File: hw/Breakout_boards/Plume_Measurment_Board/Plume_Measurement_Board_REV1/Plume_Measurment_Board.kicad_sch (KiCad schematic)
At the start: 19 parts, among them U2 LMP7721MA/NOPB, U3 LMP2022MA/NOPB, U4 AD8475ARMZ, U5 AD8475ARMZ, U7 AD7176-2BRUZ

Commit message: Schematic Progress Buffer/2nd Stage Amplifier Integration
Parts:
- added C14: 10uF, Capacitor_SMD:C_0805_2012Metric_Pad1.18x1.45mm_HandSolder, symbol Device:C
- added C15: 100nF, Capacitor_SMD:C_0603_1608Metric_Pad1.08x0.95mm_HandSolder, symbol Device:C
- added C16: 1uF, Capacitor_SMD:C_0805_2012Metric_Pad1.18x1.45mm_HandSolder, symbol Device:C
- added R10, R9: ?, Resistor_SMD:R_0603_1608Metric_Pad0.98x0.95mm_HandSolder, symbol Device:R_US
- added R11, R12: 1000, Resistor_SMD:R_0603_1608Metric_Pad0.98x0.95mm_HandSolder, symbol Device:R_US
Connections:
- net VSS is gone; now on net GND: C11.2, C12.1, C13.1, C4.2, U7.6 (AVSS)
- net +2.5V: now also U3.3 (INA+), U4.1 (IN0.8X-), U5.1 (IN0.8X-)
- net +3V3: now also U7.16 (IOVDD), C14.2, C15.2
- net +5V: now also U3.8 (V+), U4.3 (VS+), U5.3 (VS+)
- net GND: now also U3.4 (V-), U4.8 (VS-), U5.8 (VS-), U7.17 (DGND), C14.1, C15.1, C16.1
- net at U7.18 (REGCAPD): now also C16.2
- net 1_IN0.8+: now reaches U4.10 (IN0.8X+)
- net 1_IN0.8+: now also U3.1 (OUTA), R11.2
- net at U3.2 (INA-): now also R11.1, R12.2
- net 2_IN0.8+: now reaches U5.10 (IN0.8X+)
- new net Amplified_Plume_1: R12.1
- no-connect marks 3 -> 12
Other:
- note added: "GND Power Connection"
- moved on the sheet: R7, R8

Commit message: Schematic Finished
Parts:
- added C17: .1pF, Capacitor_SMD:C_0402_1005Metric_Pad0.74x0.62mm_HandSolder, symbol Device:C
- added R13: 1G, Resistor_SMD:R_2512_6332Metric_Pad1.40x3.35mm_HandSolder, symbol Device:R_US
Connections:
- net +2.5V: now also U2.2 (NC), U2.7 (NC), U3.5 (INB+)
- net +5V: now also U2.6 (V+)
- net 2_IN0.8+: now also R9.2, U3.7 (OUTB)
- net Amplified_Plume_1: now also R10.1, U2.4 (OUT), C17.2, R13.1
- net GND: now also U2.1 (IN+), U2.3 (V-)
- net Plume: now also U2.8 (IN-), C17.1, R13.2
- net at U3.6 (INB-): now also R10.2, R9.1
- no-connect marks 12 -> 13
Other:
- moved on the sheet: R10, R9, U2

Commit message: Good Routing Progress
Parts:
- added C18: 1uF, Capacitor_SMD:C_0805_2012Metric_Pad1.18x1.45mm_HandSolder, symbol Device:C
- added C19: 1uF, Capacitor_SMD:C_0603_1608Metric_Pad1.08x0.95mm_HandSolder, symbol Device:C
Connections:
- net +2.5V: now also C10.1, C5.2, C6.1, C9.2, C18.2, C19.1
- net +5V: now also C19.2
- net GND: now also C18.1; no longer C10.1, C5.2, C6.1, C9.2
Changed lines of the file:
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@@
 	)
 	(junction
+		(at 110.49 180.34)
+		(diameter 0)
+		(color 0 0 0 0)
+	)
+	(junction
 		(at 175.26 125.73)
 		(diameter 0)
@@
 	(wire
 		(pts
+			(xy 110.49 168.91) (xy 110.49 171.45)
+		)
+		(stroke
+			(width 0)
+			(type default)
+		)
+	)
+	(wire
+		(pts
 			(xy 74.93 34.29) (xy 74.93 53.34)
 		)
@@
 	(wire
 		(pts
+			(xy 110.49 189.23) (xy 110.49 194.31)
+		)
+		(stroke
+			(width 0)
+			(type default)
+		)
+	)
+	(wire
+		(pts
 			(xy 262.89 113.03) (xy 262.89 114.3)
 		)
@@
 	(wire
 		(pts
+			(xy 110.49 180.34) (xy 110.49 181.61)
+		)
+		(stroke
+			(width 0)
+			(type default)
+		)
+	)
+	(wire
+		(pts
 			(xy 62.23 26.67) (xy 74.93 26.67)
 		)
@@
 	(wire
 		(pts
+			(xy 102.87 180.34) (xy 110.49 180.34)
+		)
+		(stroke
+			(width 0)
+			(type default)
+		)
+	)
+	(wire
+		(pts
 			(xy 91.44 111.76) (xy 96.52 111.76)
 		)
@@
 	(wire
 		(pts
+			(xy 110.49 179.07) (xy 110.49 180.34)
+		)
+		(stroke
+			(width 0)
+			(type default)
+		)
+	)
+	(wire
+		(pts
 			(xy 147.32 97.79) (xy 147.32 100.33)
 		)
@@
 		)
 	)
+	(hierarchical_label "+2.5V"
+		(shape input)
+		(at 269.24 93.98 0)
+		(effects
+			(font
+				(size 1.27 1.27)
+			)
+			(justify left)
+		)
+	)
 	(hierarchical_label "VSS"
 		(shape input)
@@
 		)
 	)
+	(hierarchical_label "+2.5V"
+		(shape input)
+		(at 274.32 114.3 0)
+		(effects
+			(font
+				(size 1.27 1.27)
+			)
+			(justify left)
+		)
+	)
+	(hierarchical_label "+2.5V"
+		(shape input)
+		(at 102.87 180.34 180)
+		(effects
+			(font
+				(size 1.27 1.27)
+			)
+			(justify right)
+		)
+	)
 	(hierarchical_label "+OUT_2"
 		(shape input)
@@
 		)
 	)
+	(hierarchical_label "VSS"
+		(shape input)
+		(at 110.49 194.31 180)
+		(effects
+			(font
+				(size 1.27 1.27)
+			)
+			(justify right)
+		)
+	)
 	(hierarchical_label "+2.5V"
 		(shape input)
@@
 	)
 	(symbol
-		(lib_id "power:GND")
-		(at 274.32 114.3 0)
+		(lib_id "power:+3V3")
+		(at 110.49 168.91 0)
 		(unit 1)
 		(body_style 1)
@@
 		(in_pos_files yes)
 		(dnp no)
-		(fields_autoplaced yes)
-		(property "Reference" "#PWR07"
-			(at 274.32 120.65 0)
+		(property "Reference" "#PWR0255"
+			(at 110.49 172.72 0)
 			(hide yes)
 			(show_name no)
@@
 			)
 		)
-		(property "Value" "GND"
-			(at 274.32 119.38 0)
+		(property "Value" "+5V"
+			(at 110.236 165.1 0)
 			(show_name no)
 			(do_not_autoplace no)
@@
 		)
 		(property "Footprint" ""
-			(at 274.32 114.3 0)
+			(at 110.49 168.91 0)
 			(hide yes)
 			(show_name no)
@@
 		)
 		(property "Datasheet" ""
-			(at 274.32 114.3 0)
+			(at 110.49 168.91 0)
 			(hide yes)
 			(show_name no)
@@
 			)
 		)
-		(property "Description" "Power symbol creates a global label with name \"GND\" , ground"
-			(at 274.32 114.3 0)
+		(property "Description" "Power symbol creates a global label with name \"+3V3\""
+			(at 110.49 168.91 0)
 			(hide yes)
 			(show_name no)
@@
 			(project "Plume_Measurment_Board"
 				(path "/2e1d3673-27b9-4604-80fb-036cec98a912"
-					(reference "#PWR07")
+					(reference "#PWR0255")
 					(unit 1)
 				)
@@
 	)
 	(symbol
+		(lib_id "Device:C")
+		(at 110.49 175.26 180)
+		(unit 1)
+		(body_style 1)
+		(exclude_from_sim no)
+		(in_bom yes)
+		(on_board yes)
+		(in_pos_files yes)
+		(dnp no)
+		(property "Reference" "C19"
+			(at 113.284 173.482 0)
+			(show_name no)
+			(do_not_autoplace no)
+			(effects
+				(font
+					(size 1.27 1.27)
+				)
+				(justify right)
+			)
+		)
+		(property "Value" "1uF"
+			(at 113.284 176.022 0)
+			(show_name no)
+			(do_not_autoplace no)
+			(effects
+				(font
+					(size 1.27 1.27)
+				)
+				(justify right)
+			)
+		)
+		(property "Footprint" "Capacitor_SMD:C_0603_1608Metric_Pad1.08x0.95mm_HandSolder"
+			(at 109.5248 171.45 0)
+			(hide yes)
+			(show_name no)
+			(do_not_autoplace no)
+			(effects
+				(font
+					(size 1.27 1.27)
+				)
+			)
+		)
+		(property "Datasheet" ""
+			(at 110.49 175.26 0)
+			(hide yes)
+			(show_name no)
+			(do_not_autoplace no)
+			(effects
+				(font
+					(size 1.27 1.27)
+				)
+			)
+		)
+		(property "Description" "Unpolarized capacitor"
+			(at 110.49 175.26 0)
+			(hide yes)
+			(show_name no)
+			(do_not_autoplace no)
+			(effects
+				(font
+					(size 1.27 1.27)
+				)
+			)
+		)
+		(pin "2"
+		)
+		(pin "1"
+		)
+		(instances
+			(project "Plume_Measurment_Board"
+				(path "/2e1d3673-27b9-4604-80fb-036cec98a912"
+					(reference "C19")
+					(unit 1)
+				)
+			)
+		)
+	)
+	(symbol
 		(lib_id "ADC_Analog_Devices:AD7176-2BRUZ")
 		(at 177.8 110.49 0)
@@
 	)
 	(symbol
+		(lib_id "Device:C")
+		(at 110.49 185.42 180)
+		(unit 1)
+		(body_style 1)
+		(exclude_from_sim no)
+		(in_bom yes)
+		(on_board yes)
+		(in_pos_files yes)
+		(dnp no)
+		(property "Reference" "C18"
+			(at 103.632 183.896 0)
+			(show_name no)
+			(do_not_autoplace no)
+			(effects
+				(font
+					(size 1.27 1.27)
+				)
+				(justify right)
+			)
+		)
+		(property "Value" "1uF"
+			(at 103.632 186.436 0)
+			(show_name no)
+			(do_not_autoplace no)
+			(effects
+				(font
+					(size 1.27 1.27)
+				)
+				(justify right)
+			)
+		)
+		(property "Footprint" "Capacitor_SMD:C_0805_2012Metric_Pad1.18x1.45mm_HandSolder"
+			(at 109.5248 181.61 0)
+			(hide yes)
+			(show_name no)
+			(do_not_autoplace no)
+			(effects
+				(font
+					(size 1.27 1.27)
+				)
+			)
+		)
+		(property "Datasheet" ""
+			(at 110.49 185.42 0)
+			(hide yes)
+			(show_name no)
+			(do_not_autoplace no)
+			(effects
+				(font
+					(size 1.27 1.27)
+				)
+			)
+		)
+		(property "Description" "Unpolarized capacitor"
+			(at 110.49 185.42 0)
+			(hide yes)
+			(show_name no)
+			(do_not_autoplace no)
+			(effects
+				(font
+					(size 1.27 1.27)
+				)
+			)
+		)
+		(pin "2"
+		)
+		(pin "1"
+		)
+		(instances
+			(project "Plume_Measurment_Board"
+				(path "/2e1d3673-27b9-4604-80fb-036cec98a912"
+					(reference "C18")
+					(unit 1)
+				)
+			)
+		)
+	)
+	(symbol
 		(lib_id "Device:R_US")
 		(at 269.24 102.87 90)
@@
 					(unit 1)
 				)
-			)
-		)
-	)
-	(symbol
-		(lib_id "power:GND")
-		(at 269.24 93.98 0)
-		(unit 1)
-		(body_style 1)
-		(exclude_from_sim no)
-		(in_bom yes)
-		(on_board yes)
-		(in_pos_files yes)
-		(dnp no)
-		(property "Reference" "#PWR06"
-			(at 269.24 100.33 0)
-			(hide yes)
-			(show_name no)
-			(do_not_autoplace no)
-			(effects
-				(font
-					(size 1.27 1.27)
-				)
-			)
-		)
-		(property "Value" "GND"
-			(at 265.43 96.012 0)
-			(show_name no)
-			(do_not_autoplace no)
-			(effects
-				(font
-					(size 1.27 1.27)
-				)
-			)
-		)
-		(property "Footprint" ""
-			(at 269.24 93.98 0)
-			(hide yes)
-			(show_name no)
-			(do_not_autoplace no)
-			(effects
-				(font
-					(size 1.27 1.27)
-				)
-			)
-		)
-		(property "Datasheet" ""
-			(at 269.24 93.98 0)
-			(hide yes)
-			(show_name no)
-			(do_not_autoplace no)
-			(effects
-				(font
-					(size 1.27 1.27)
-				)
-			)
-		)
-		(property "Description" "Power symbol creates a global label with name \"GND\" , ground"
-			(at 269.24 93.98 0)
-			(hide yes)
-			(show_name no)
-			(do_not_autoplace no)
-			(effects
-				(font
-					(size 1.27 1.27)
-				)
-			)
-		)
-		(pin "1"
-		)
-		(instances
-			(project "Plume_Measurment_Board"
-				(path "/2e1d3673-27b9-4604-80fb-036cec98a912"
-					(reference "#PWR06")
-					(unit 1)
-				)

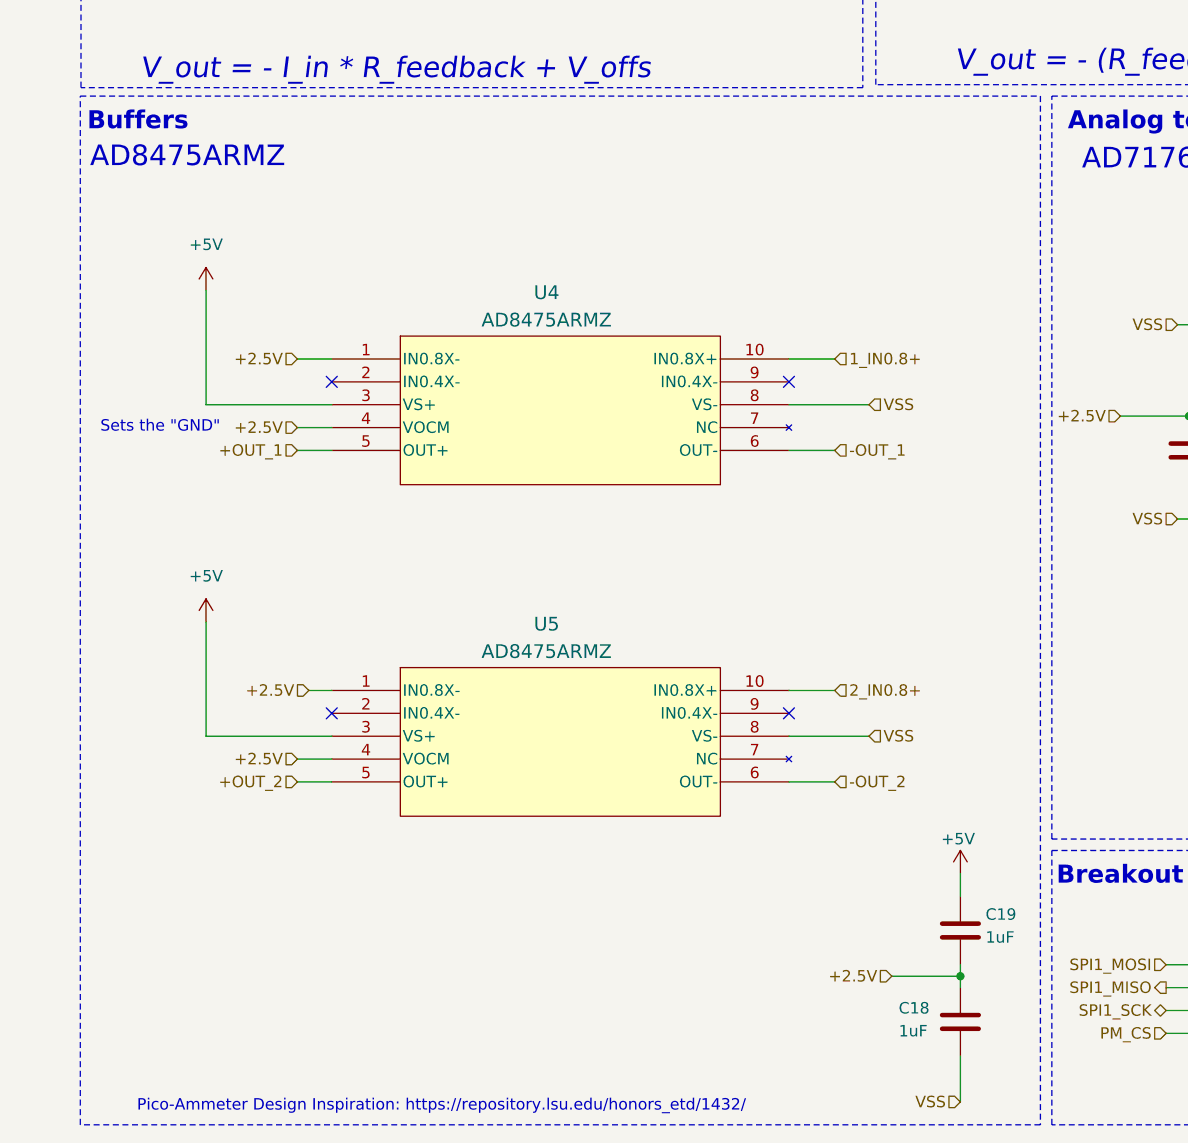
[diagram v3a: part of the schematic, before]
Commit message: MAX31856 Driver Full Integrations
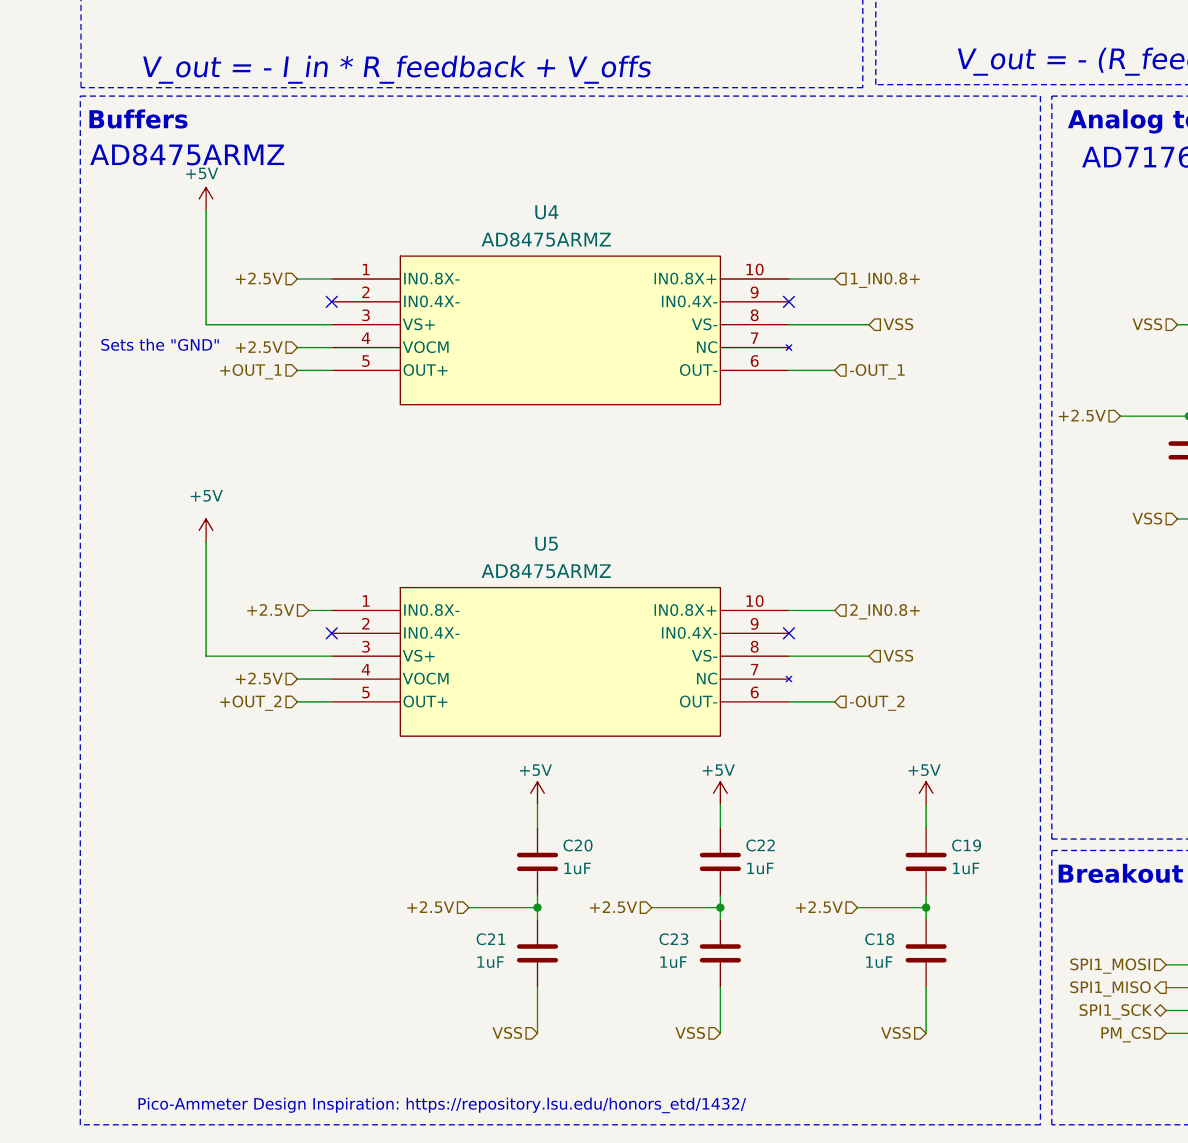
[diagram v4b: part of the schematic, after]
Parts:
- added C20, C22: 1uF, Capacitor_SMD:C_0603_1608Metric_Pad1.08x0.95mm_HandSolder, symbol Device:C
- added C21, C23: 1uF, Capacitor_SMD:C_0805_2012Metric_Pad1.18x1.45mm_HandSolder, symbol Device:C
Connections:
- net +2.5V: now also C20.1, C21.2, C22.1, C23.2
- net +5V: now also C20.2, C22.2
- net GND: now also C21.1, C23.1
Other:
- moved on the sheet: C18, C19, U4, U5

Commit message: 2nd Stage Amp Routing Progress
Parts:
- R10, R9: value ? -> 1000; now fitted
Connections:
- net 1_IN0.8+: now also R9.2, U3.7 (OUTB); no longer R11.2, U3.1 (OUTA)
- net 2_IN0.8+: now also R11.2, U3.1 (OUTA); no longer R9.2, U3.7 (OUTB)
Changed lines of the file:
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@@
 	)
 	(junction
-		(at 149.86 41.91)
+		(at 209.55 46.99)
+		(diameter 0)
+		(color 0 0 0 0)
+	)
+	(junction
+		(at 209.55 55.88)
 		(diameter 0)
 		(color 0 0 0 0)
@@
 	)
 	(junction
-		(at 209.55 46.99)
+		(at 149.86 41.91)
 		(diameter 0)
 		(color 0 0 0 0)
@@
 		(color 0 0 0 0)
 	)
-	(junction
-		(at 209.55 55.88)
-		(diameter 0)
-		(color 0 0 0 0)
-	)
 	(no_connect
 		(at 224.79 133.35)
@@
 	(wire
 		(pts
-			(xy 187.96 57.15) (xy 194.31 57.15)
+			(xy 193.04 59.69) (xy 194.31 59.69)
 		)
 		(stroke
@@
 	(wire
 		(pts
+			(xy 209.55 48.26) (xy 209.55 46.99)
+		)
+		(stroke
+			(width 0)
+			(type default)
+		)
+	)
+	(wire
+		(pts
 			(xy 36.83 149.86) (xy 40.64 149.86)
 		)
@@
 	(wire
 		(pts
-			(xy 133.35 179.07) (xy 135.89 179.07)
+			(xy 193.04 59.69) (xy 193.04 57.15)
 		)
 		(stroke
@@
 	(wire
 		(pts
-			(xy 209.55 54.61) (xy 209.55 55.88)
+			(xy 133.35 179.07) (xy 135.89 179.07)
 		)
 		(stroke
@@
 	(wire
 		(pts
+			(xy 193.04 57.15) (xy 187.96 57.15)
+		)
+		(stroke
+			(width 0)
+			(type default)
+		)
+	)
+	(wire
+		(pts
 			(xy 274.32 30.48) (xy 274.32 35.56)
 		)
@@
 		)
 	)
-	(hierarchical_label "1_IN0.8+"
-		(shape input)
-		(at 147.32 41.91 180)
-		(effects
-			(font
-				(size 1.27 1.27)
-			)
-			(justify right)
-		)
-	)
 	(hierarchical_label "VSS"
 		(shape input)
@@
 	(hierarchical_label "1_IN0.8+"
 		(shape input)
+		(at 209.55 40.64 0)
+		(effects
+			(font
+				(size 1.27 1.27)
+			)
+			(justify left)
+		)
+	)
+	(hierarchical_label "1_IN0.8+"
+		(shape input)
 		(at 96.52 102.87 0)
 		(effects
@@
 		)
 	)
-	(hierarchical_label "Amplified_Plume_1"
-		(shape output)
-		(at 209.55 69.85 0)
-		(effects
-			(font
-				(size 1.27 1.27)
-			)
-			(justify left)
-		)
-	)
 	(hierarchical_label "-OUT_1"
 		(shape input)
@@
 	(hierarchical_label "+2.5V"
 		(shape input)
-		(at 194.31 57.15 0)
+		(at 194.31 59.69 0)
 		(effects
 			(font
@@
 		)
 	)
-	(hierarchical_label "2_IN0.8+"
-		(shape input)
-		(at 209.55 40.64 0)
-		(effects
-			(font
-				(size 1.27 1.27)
-			)
-			(justify left)
-		)
-	)
 	(hierarchical_label "+2.5V"
 		(shape input)
@@
 		)
 	)
+	(hierarchical_label "Amplified_Plume_1"
+		(shape output)
+		(at 209.55 69.85 0)
+		(effects
+			(font
+				(size 1.27 1.27)
+			)
+			(justify left)
+		)
+	)
 	(hierarchical_label "PM_CS"
 		(shape input)
@@
 		)
 	)
+	(hierarchical_label "2_IN0.8+"
+		(shape input)
+		(at 147.32 41.91 180)
+		(effects
+			(font
+				(size 1.27 1.27)
+			)
+			(justify right)
+		)
+	)
 	(hierarchical_label "VSS"
 		(shape input)
@@
 	(symbol
 		(lib_id "Device:R_US")
-		(at 209.55 50.8 180)
+		(at 209.55 52.07 180)
 		(unit 1)
 		(body_style 1)
@@
 		(on_board yes)
 		(in_pos_files yes)
-		(dnp yes)
+		(dnp no)
 		(property "Reference" "R9"
-			(at 212.471 51.689 0)
+			(at 214.63 53.086 0)
 			(show_name no)
 			(do_not_autoplace no)
@@
 			)
 		)
-		(property "Value" "?"
-			(at 212.471 49.657 0)
+		(property "Value" "1000"
+			(at 214.249 50.927 0)
 			(show_name no)
 			(do_not_autoplace no)
@@
 		)
 		(property "Footprint" "Resistor_SMD:R_0603_1608Metric_Pad0.98x0.95mm_HandSolder"
-			(at 208.534 50.546 90)
+			(at 208.534 51.816 90)
 			(hide yes)
 			(show_name no)
@@
 		)
 		(property "Datasheet" ""
-			(at 209.55 50.8 0)
+			(at 209.55 52.07 0)
 			(hide yes)
 			(show_name no)
@@
 		)
 		(property "Description" "Resistor, US symbol"
-			(at 209.55 50.8 0)
+			(at 209.55 52.07 0)
 			(hide yes)
 			(show_name no)
@@
 		(on_board yes)
 		(in_pos_files yes)
-		(dnp yes)
+		(dnp no)
 		(property "Reference" "R10"
-			(at 212.471 61.849 0)
+			(at 214.884 61.976 0)
 			(show_name no)
 			(do_not_autoplace no)
@@
 			)
 		)
-		(property "Value" "?"
-			(at 212.471 59.817 0)
+		(property "Value" "1000"
+			(at 214.884 59.944 0)
 			(show_name no)
 			(do_not_autoplace no)

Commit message: First + Second Stage Amp Work
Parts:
- R11, R12: now not fitted
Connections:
- net +2.5V: now also U2.1 (IN+)
- net GND: no longer U2.1 (IN+)
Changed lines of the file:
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@@
 	(wire
 		(pts
-			(xy 163.83 182.88) (xy 165.1 182.88)
+			(xy 27.94 55.88) (xy 27.94 60.96)
 		)
 		(stroke
@@
 	(wire
 		(pts
-			(xy 27.94 55.88) (xy 27.94 58.42)
+			(xy 163.83 182.88) (xy 165.1 182.88)
 		)
 		(stroke
@@
 		)
 	)
+	(hierarchical_label "+2.5V"
+		(shape input)
+		(at 27.94 60.96 180)
+		(effects
+			(font
+				(size 1.27 1.27)
+			)
+			(justify right)
+		)
+	)
 	(hierarchical_label "2_IN0.8+"
 		(shape input)
@@
 		(on_board yes)
 		(in_pos_files yes)
-		(dnp no)
+		(dnp yes)
 		(property "Reference" "R11"
 			(at 131.318 41.402 0)
@@
 	)
 	(symbol
-		(lib_id "power:GND")
-		(at 27.94 58.42 0)
-		(unit 1)
-		(body_style 1)
-		(exclude_from_sim no)
-		(in_bom yes)
-		(on_board yes)
-		(in_pos_files yes)
-		(dnp no)
-		(fields_autoplaced yes)
-		(property "Reference" "#PWR08"
-			(at 27.94 64.77 0)
-			(hide yes)
-			(show_name no)
-			(do_not_autoplace no)
-			(effects
-				(font
-					(size 1.27 1.27)
-				)
-			)
-		)
-		(property "Value" "GND"
-			(at 27.94 63.5 0)
-			(show_name no)
-			(do_not_autoplace no)
-			(effects
-				(font
-					(size 1.27 1.27)
-				)
-			)
-		)
-		(property "Footprint" ""
-			(at 27.94 58.42 0)
-			(hide yes)
-			(show_name no)
-			(do_not_autoplace no)
-			(effects
-				(font
-					(size 1.27 1.27)
-				)
-			)
-		)
-		(property "Datasheet" ""
-			(at 27.94 58.42 0)
-			(hide yes)
-			(show_name no)
-			(do_not_autoplace no)
-			(effects
-				(font
-					(size 1.27 1.27)
-				)
-			)
-		)
-		(property "Description" "Power symbol creates a global label with name \"GND\" , ground"
-			(at 27.94 58.42 0)
-			(hide yes)
-			(show_name no)
-			(do_not_autoplace no)
-			(effects
-				(font
-					(size 1.27 1.27)
-				)
-			)
-		)
-		(pin "1"
-		)
-		(instances
-			(project "Plume_Measurment_Board"
-				(path "/2e1d3673-27b9-4604-80fb-036cec98a912"
-					(reference "#PWR08")
-					(unit 1)
-				)
-			)
-		)
-	)
-	(symbol
 		(lib_id "Device:C")
 		(at 135.89 121.92 0)
@@
 		(on_board yes)
 		(in_pos_files yes)
-		(dnp no)
+		(dnp yes)
 		(property "Reference" "R12"
 			(at 131.318 55.626 0)

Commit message: Entire RF pipeline
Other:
- sheet Connectors ports: added +2.5V; removed none
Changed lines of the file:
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@@
 		)
 	)
+	(wire
+		(pts
+			(xy 163.83 189.23) (xy 167.64 189.23)
+		)
+		(stroke
+			(width 0)
+			(type default)
+		)
+	)
 	(hierarchical_label "VSS"
 		(shape input)
@@
 		)
 	)
+	(hierarchical_label "+2.5V"
+		(shape input)
+		(at 167.64 189.23 0)
+		(effects
+			(font
+				(size 1.27 1.27)
+			)
+			(justify left)
+		)
+	)
 	(hierarchical_label "VSS"
 		(shape input)
@@
 			(effects
 				(font
+					(size 1.27 1.27)
+				)
+				(justify right)
+			)
+		)
+		(pin "+2.5V" input
+			(at 163.83 189.23 0)
+			(effects
+				(font
